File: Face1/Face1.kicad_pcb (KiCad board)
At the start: 2 copper layers, 149.9 x 149.9 mm, 28 parts

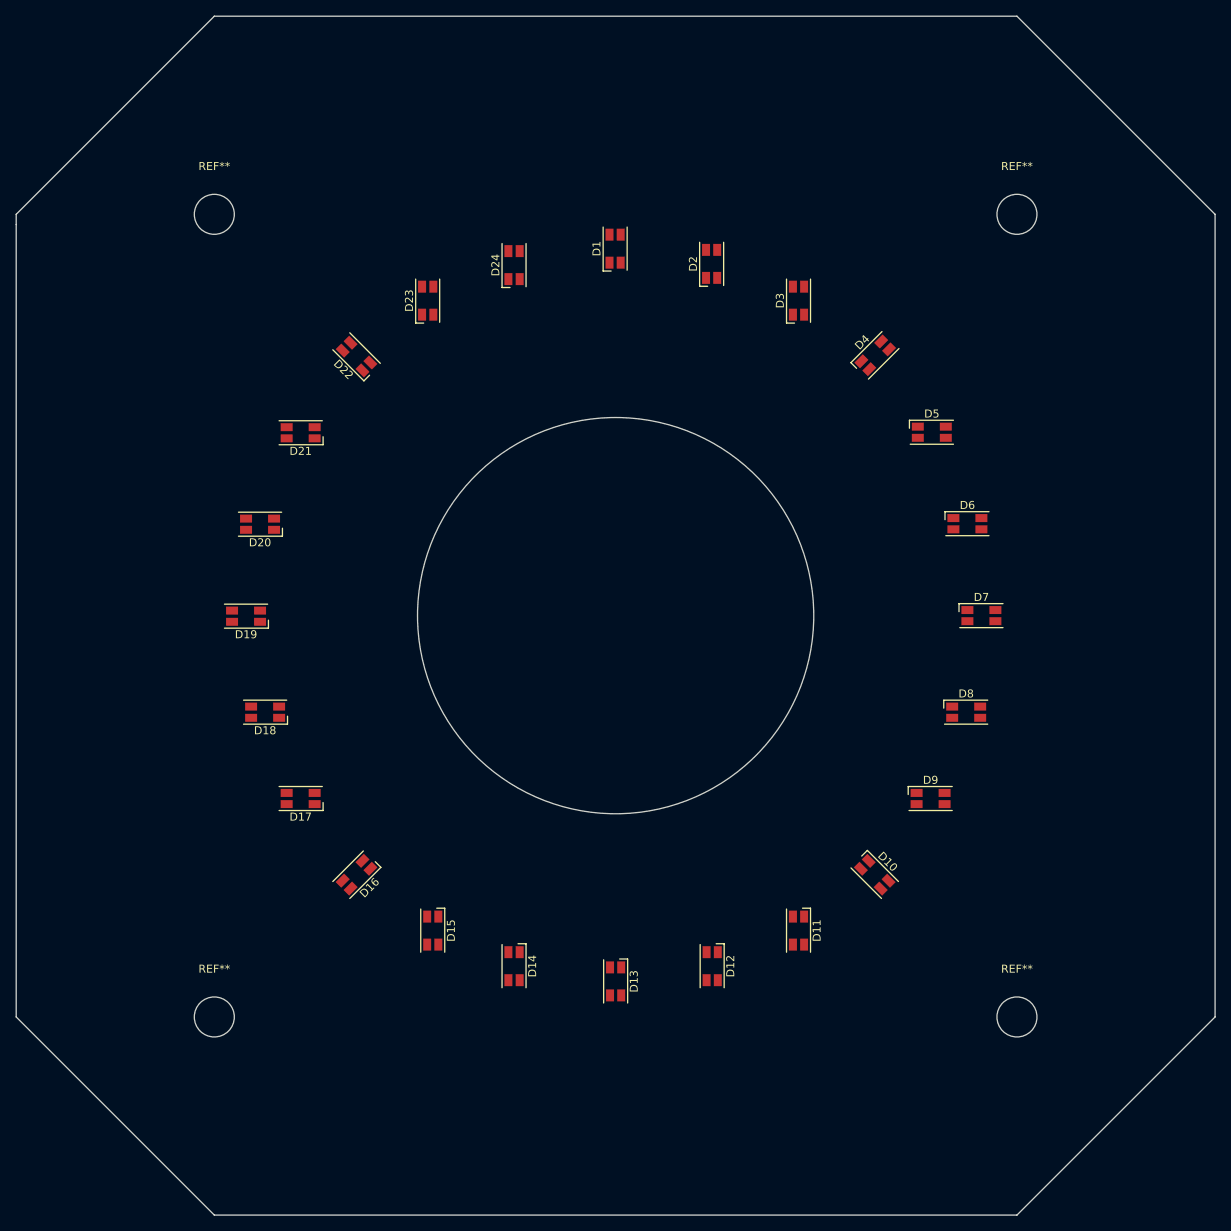
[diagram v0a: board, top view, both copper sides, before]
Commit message: Changed to multiple AS1105 for LED drivers
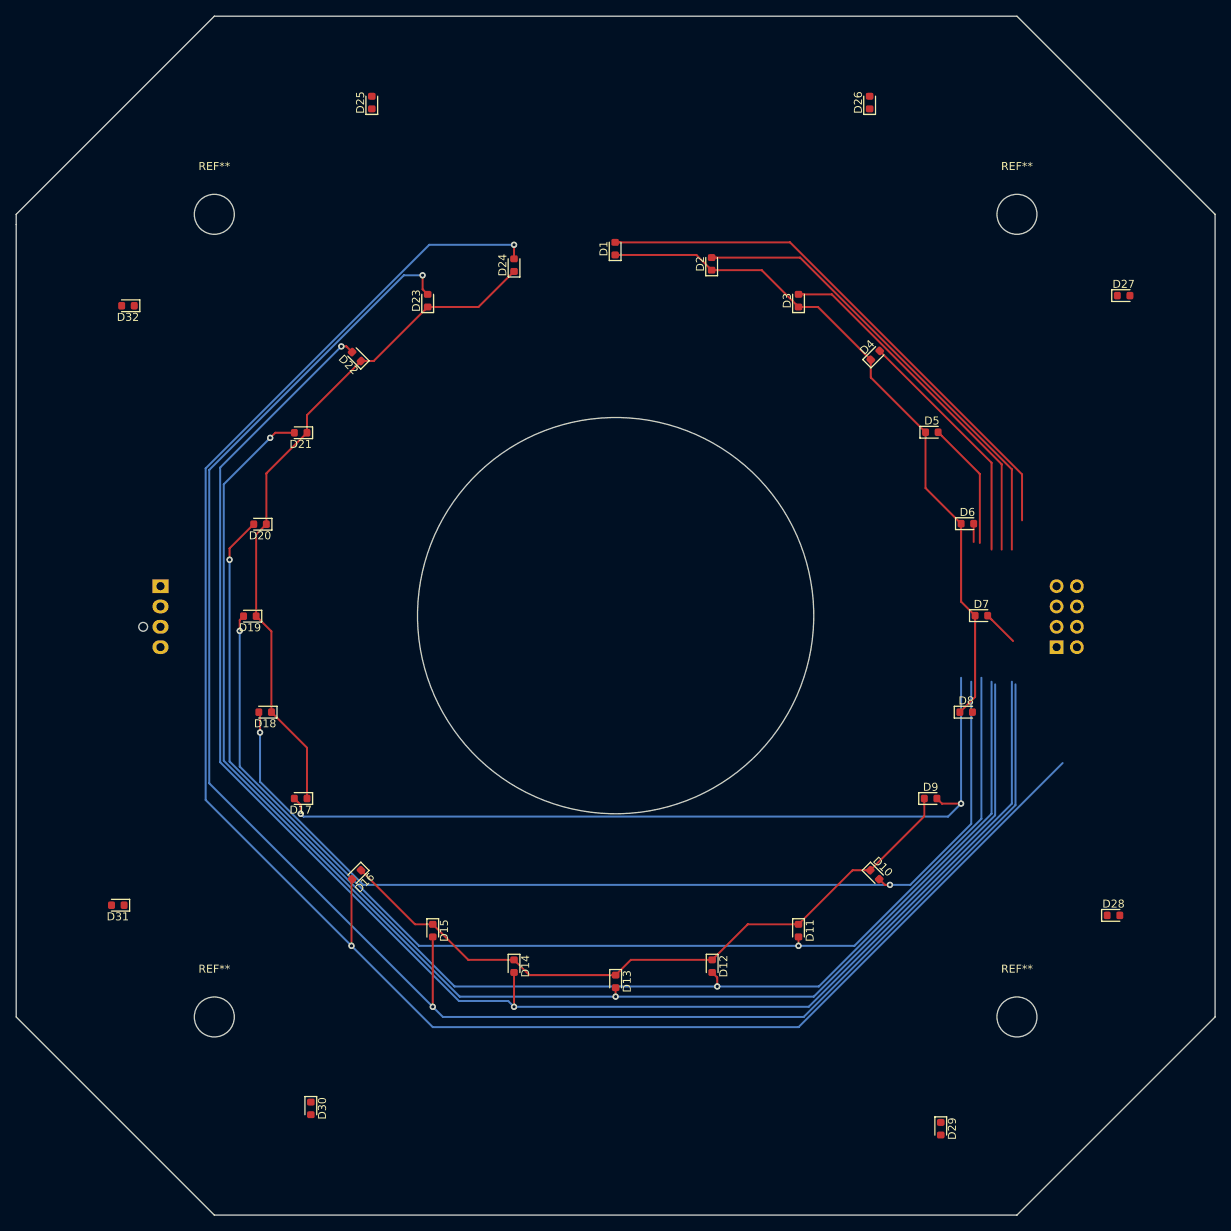
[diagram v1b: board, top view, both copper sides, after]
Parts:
- added D25: LED, LED_SMD:LED_0603_1608Metric, F.Cu at (63.5, 29.2)
- added D26: LED, LED_SMD:LED_0603_1608Metric, F.Cu at (125.7, 29.2)
- added D27: LED, LED_SMD:LED_0603_1608Metric, F.Cu at (157.5, 53.3)
- added D28: LED, LED_SMD:LED_0603_1608Metric, F.Cu at (156.2, 130.8)
- added D29: LED, LED_SMD:LED_0603_1608Metric, F.Cu at (134.6, 157.5)
- added D30: LED, LED_SMD:LED_0603_1608Metric, F.Cu at (55.9, 154.9)
- added D31: LED, LED_SMD:LED_0603_1608Metric, F.Cu at (31.8, 129.5)
- added D32: LED, LED_SMD:LED_0603_1608Metric, F.Cu at (33.0, 54.6)
- added J1: Conn_02x04_Odd_Even, Connector_IDC:IDC-Header_2x04_P2.54mm_Vertical, B.Cu at (149.1, 97.3)
- added J2: Conn_01x04_Male, Connector:FanPinHeader_1x04_P2.54mm_Vertical, B.Cu at (37.1, 89.7)
- D1, D10, D11, D12, D13, D14, D15, D16, D17, D18, D19, D2, D20, D21, D22, D23, D24, D3, D4, D5, D6, D7, D8, D9: value LED_Dual_AACC_pins -> LED; footprint LED_SMD:LED_RGB_1210 -> LED_SMD:LED_0603_1608Metric
- moved D19 0.48 mm to (48.3, 93.4)
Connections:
- D1 pad 1: Net-(D1-Pad1) -> DIG0
- D1 pad 2: Net-(D1-Pad2) -> SEGA
- D10 pad 1: Net-(D10-Pad1) -> DIG1
- D10 pad 2: Net-(D10-Pad2) -> SEGB
- D11 pad 1: Net-(D11-Pad1) -> DIG1
- D11 pad 2: Net-(D11-Pad2) -> SEGC
- D12 pad 1: Net-(D12-Pad1) -> DIG1
- D12 pad 2: Net-(D12-Pad2) -> SEGD
- D13 pad 1: Net-(D13-Pad1) -> DIG1
- D13 pad 2: Net-(D13-Pad2) -> SEGE
- D14 pad 1: Net-(D14-Pad1) -> DIG1
- D14 pad 2: Net-(D14-Pad2) -> SEGF
- D15 pad 1: Net-(D15-Pad1) -> DIG1
- D15 pad 2: Net-(D15-Pad2) -> SEGG
- D16 pad 1: Net-(D16-Pad1) -> DIG1
- D16 pad 2: Net-(D16-Pad2) -> SEGDP
- D17 pad 1: Net-(D17-Pad1) -> DIG2
- D17 pad 2: Net-(D17-Pad2) -> SEGA
- D18 pad 1: Net-(D18-Pad1) -> DIG2
- D18 pad 2: Net-(D18-Pad2) -> SEGB
- D19 pad 1: Net-(D19-Pad1) -> DIG2
- D19 pad 2: Net-(D19-Pad2) -> SEGC
- D2 pad 1: Net-(D2-Pad1) -> DIG0
- D2 pad 2: Net-(D2-Pad2) -> SEGB
- D20 pad 1: Net-(D20-Pad1) -> DIG2
- D20 pad 2: Net-(D20-Pad2) -> SEGD
- D21 pad 1: Net-(D21-Pad1) -> DIG2
- D21 pad 2: Net-(D21-Pad2) -> SEGE
- D22 pad 1: Net-(D22-Pad1) -> DIG2
- D22 pad 2: Net-(D22-Pad2) -> SEGF
- D23 pad 1: Net-(D23-Pad1) -> DIG2
- D23 pad 2: Net-(D23-Pad2) -> SEGG
- D24 pad 1: Net-(D24-Pad1) -> DIG2
- D24 pad 2: Net-(D24-Pad2) -> SEGDP
- D3 pad 1: Net-(D3-Pad1) -> DIG0
- D3 pad 2: Net-(D3-Pad2) -> SEGC
- D4 pad 1: Net-(D4-Pad1) -> DIG0
- D4 pad 2: Net-(D4-Pad2) -> SEGD
- D5 pad 1: Net-(D5-Pad1) -> DIG0
- D5 pad 2: Net-(D5-Pad2) -> SEGE
- D6 pad 1: Net-(D6-Pad1) -> DIG0
- D6 pad 2: Net-(D6-Pad2) -> SEGF
- D7 pad 1: Net-(D7-Pad1) -> DIG0
- D7 pad 2: Net-(D7-Pad2) -> SEGG
- D8 pad 1: Net-(D8-Pad1) -> DIG0
- D8 pad 2: Net-(D8-Pad2) -> SEGDP
- D9 pad 1: Net-(D9-Pad1) -> DIG1
- D9 pad 2: Net-(D9-Pad2) -> SEGA
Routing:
- net SEGDP: track 0.00 -> 234.3 mm, vias 0 -> 2
- net SEGG: track 0.00 -> 230.7 mm, vias 0 -> 2
- net SEGF: track 0.00 -> 203.9 mm, vias 0 -> 2
- net SEGE: track 0.00 -> 197.6 mm, vias 0 -> 2
- net SEGD: track 0.00 -> 195.9 mm, vias 0 -> 2
- net SEGC: track 0.00 -> 191.2 mm, vias 0 -> 2
- net SEGB: track 0.00 -> 184.1 mm, vias 0 -> 2
- net SEGA: track 0.00 -> 173.2 mm, vias 0 -> 2
- net DIG0: track 0.00 -> 87.6 mm
- net DIG2: track 0.00 -> 86.5 mm
- net DIG1: track 0.00 -> 86.3 mm
